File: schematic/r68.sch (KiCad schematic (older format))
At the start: 141 parts, among them K0 K_ESC, K0A1 K_0, K0B1 K_MIN, K0C1 K_EQL, K0D1 K_BS, K1 K_1, K10 K_TAB, K11 K_Q, K12 K_W, K13 K_E, K14 K_R, K15 K_T, K16 K_Y, K17 K_U, K18 K_I, K19 K_O, K1A1 K_P, K1B1 K_OBR, K1C1 K_CBR, K1D1 K_BSL, K2 K_2, K20 K_CAP, K21 K_A, K22 K_S, K23 K_D, K24 K_F, K25 K_G, K26 K_H, K27 K_J, K28 K_K, K29 K_L, K2A1 K_COL, K2B1 K_QOT, K2C1 K_ENT, K3 K_3, K30 K_LSH, K31 K_Z, K32 K_X, K33 K_C, K34 K_V, K35 K_B, K36 K_N, K37 K_M, K38 K_COM, K39 K_DOT, K3A1 K_QUE, K3B1 K_RSH, K4 K_4, K40 K_LCL, K41 K_LWN, K42 K_LAL, K45 K_SP, K48 K_RFN, K49 K_RALT, K4A1 K_RWIN, K4B1 K_RCTL, K5 K_5, K6 K_6, K7 K_7, K8 K_8, K9 K_9, P1 USB_B, P2 SPKR, SW1 SW_Push, U1 ATmega32U4-AU, Y1 16MHz

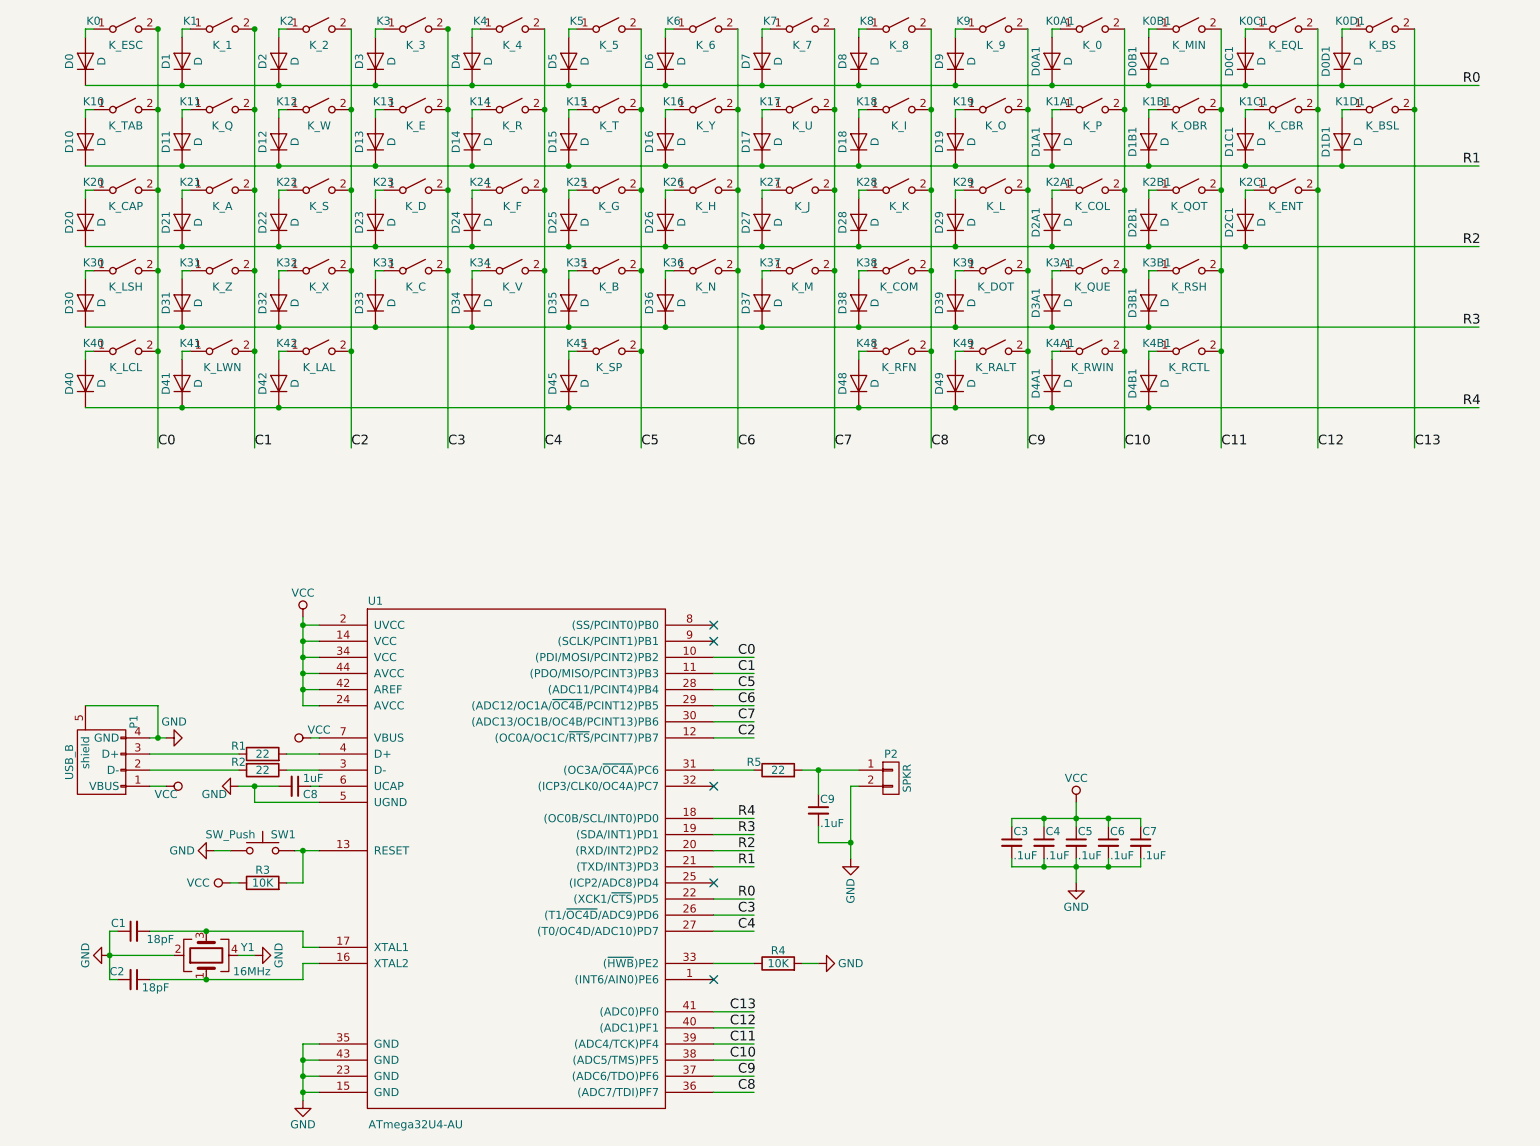
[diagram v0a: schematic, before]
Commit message: route for 68 key
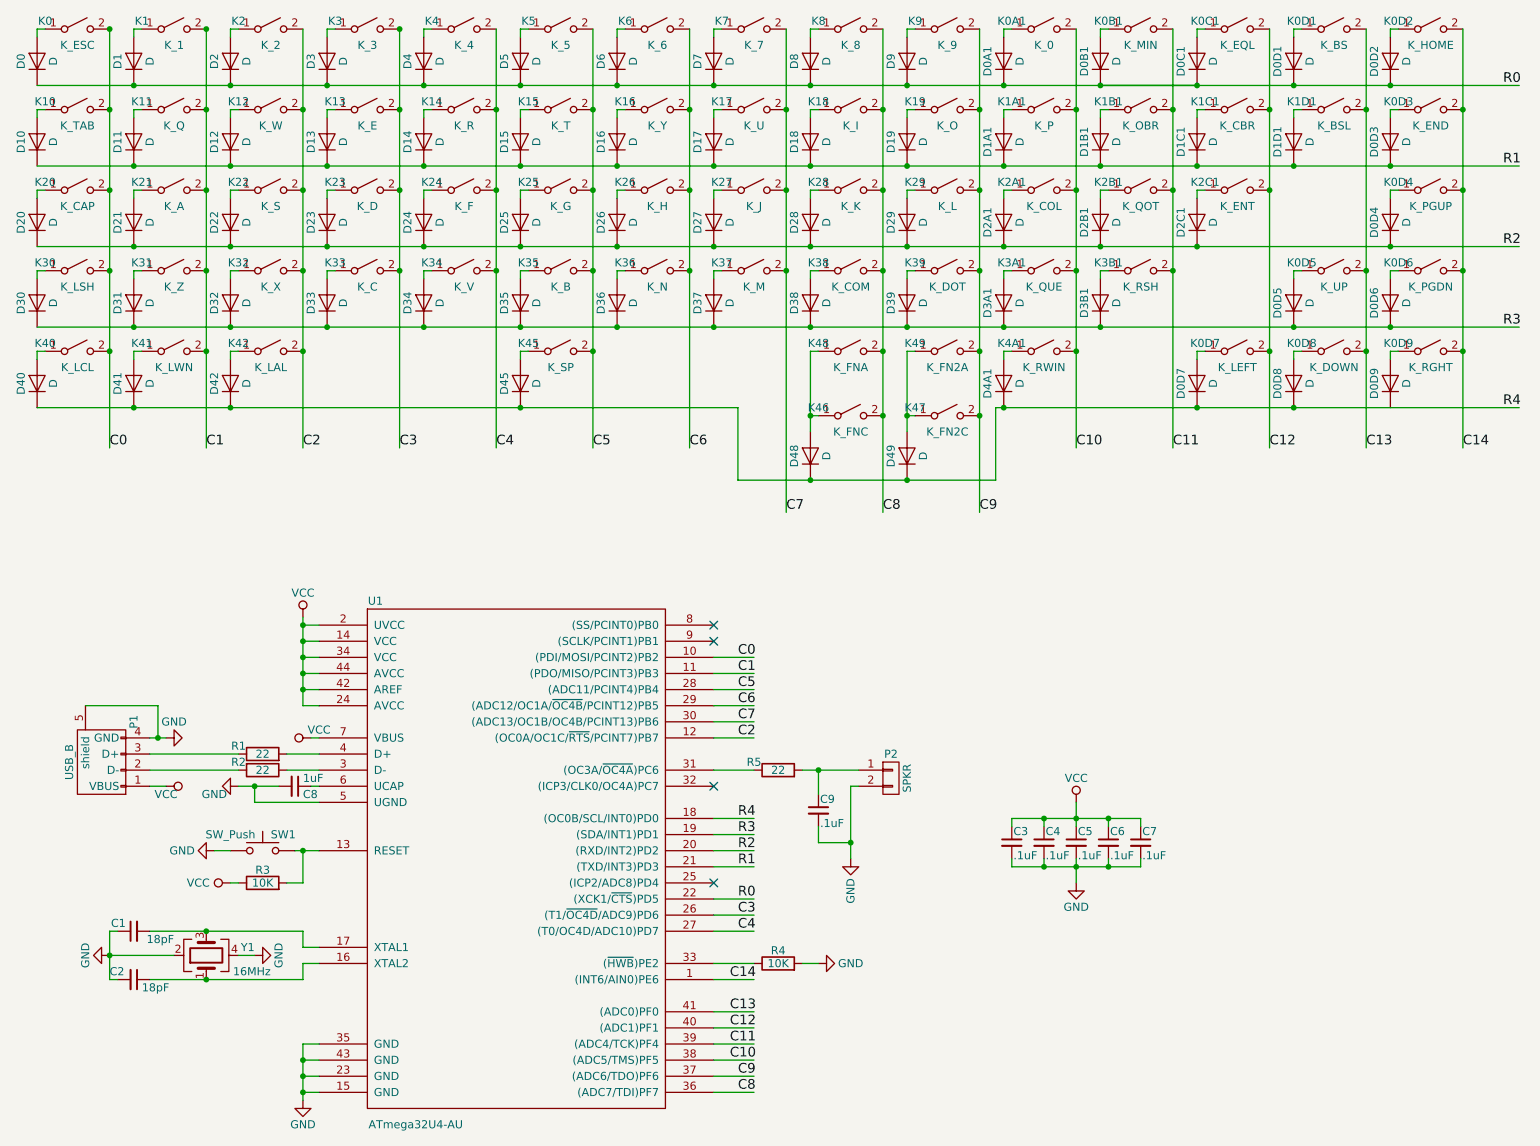
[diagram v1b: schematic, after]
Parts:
- removed D4B1: D, Diodes_SMD:D_SOD-323, symbol D
- removed K4B1: K_RCTL, Keyboard:CHERRY_PCB_125H, symbol SW_SPST
- added D0D2, D0D3, D0D4, D0D5, D0D6, D0D7, D0D8, D0D9: D, Diodes_SMD:D_SOD-323, symbol D
- added K0D2: K_HOME, Keyboard:CHERRY_PCB_100H, symbol SW_SPST
- added K0D3: K_END, Keyboard:CHERRY_PCB_100H, symbol SW_SPST
- added K0D4: K_PGUP, Keyboard:CHERRY_PCB_100H, symbol SW_SPST
- added K0D5: K_UP, Keyboard:CHERRY_PCB_100H, symbol SW_SPST
- added K0D6: K_PGDN, Keyboard:CHERRY_PCB_100H, symbol SW_SPST
- added K0D7: K_LEFT, Keyboard:CHERRY_PCB_100H, symbol SW_SPST
- added K0D8: K_DOWN, Keyboard:CHERRY_PCB_100H, symbol SW_SPST
- added K0D9: K_RGHT, Keyboard:CHERRY_PCB_100H, symbol SW_SPST
- added K46: K_FNC, Keyboard:CHERRY_PCB_100H, symbol SW_SPST
- added K47: K_FN2C, Keyboard:CHERRY_PCB_100H, symbol SW_SPST
- K3B1: footprint Keyboard:CHERRY_PCB_275H -> Keyboard:CHERRY_PCB_175H
- K48: value K_RFN -> K_FNA
- K49: value K_RALT -> K_FN2A
- K4A1: footprint Keyboard:CHERRY_PCB_125H -> Keyboard:CHERRY_PCB_100H
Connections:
- net labels added: C14
- wire segments 223 -> 245
- no-connect marks 5 -> 4
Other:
- moved on the sheet: D0, D0A1, D0B1, D0C1, D0D1, D1, D10, D11, D12, D13, D14, D15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

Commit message: Minor fixes
* fix right arrow that wasn't wired to r4
* change the diode footprint to 0805
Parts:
- D0, D0A1, D0B1, D0C1, D0D1, D0D2, D0D3, D0D4, D0D5, D0D6, D0D7, D0D8, D0D9, D1, D10, D11, D12, D13, D14, D15, D16, D17, D18, D19, D1A1, D1B1, D1C1, D1D1, D2, D20, D21, D22, D23, D24, D25, D26, D27, D28, D29, D2A1, D2B1, D2C1, D3, D30, D31, D32, D33, D34, D35, D36, D37, D38, D39, D3A1, D3B1, D4, D40, D41, D42, D45, D48, D49, D4A1, D5, D6, D7, D8, D9: footprint Diodes_SMD:D_SOD-323 -> Diodes_SMD:D_0805
